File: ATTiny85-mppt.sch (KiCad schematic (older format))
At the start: 51 parts, among them J1 S+, J2 S-, J3 O+, J4 O-, Q1 BUK9511-55A127, Q2 BUK9511-55A127, Q3 2N2222A, Q4 2N2222A, Q5 2N2907A, Q6 2N2222A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

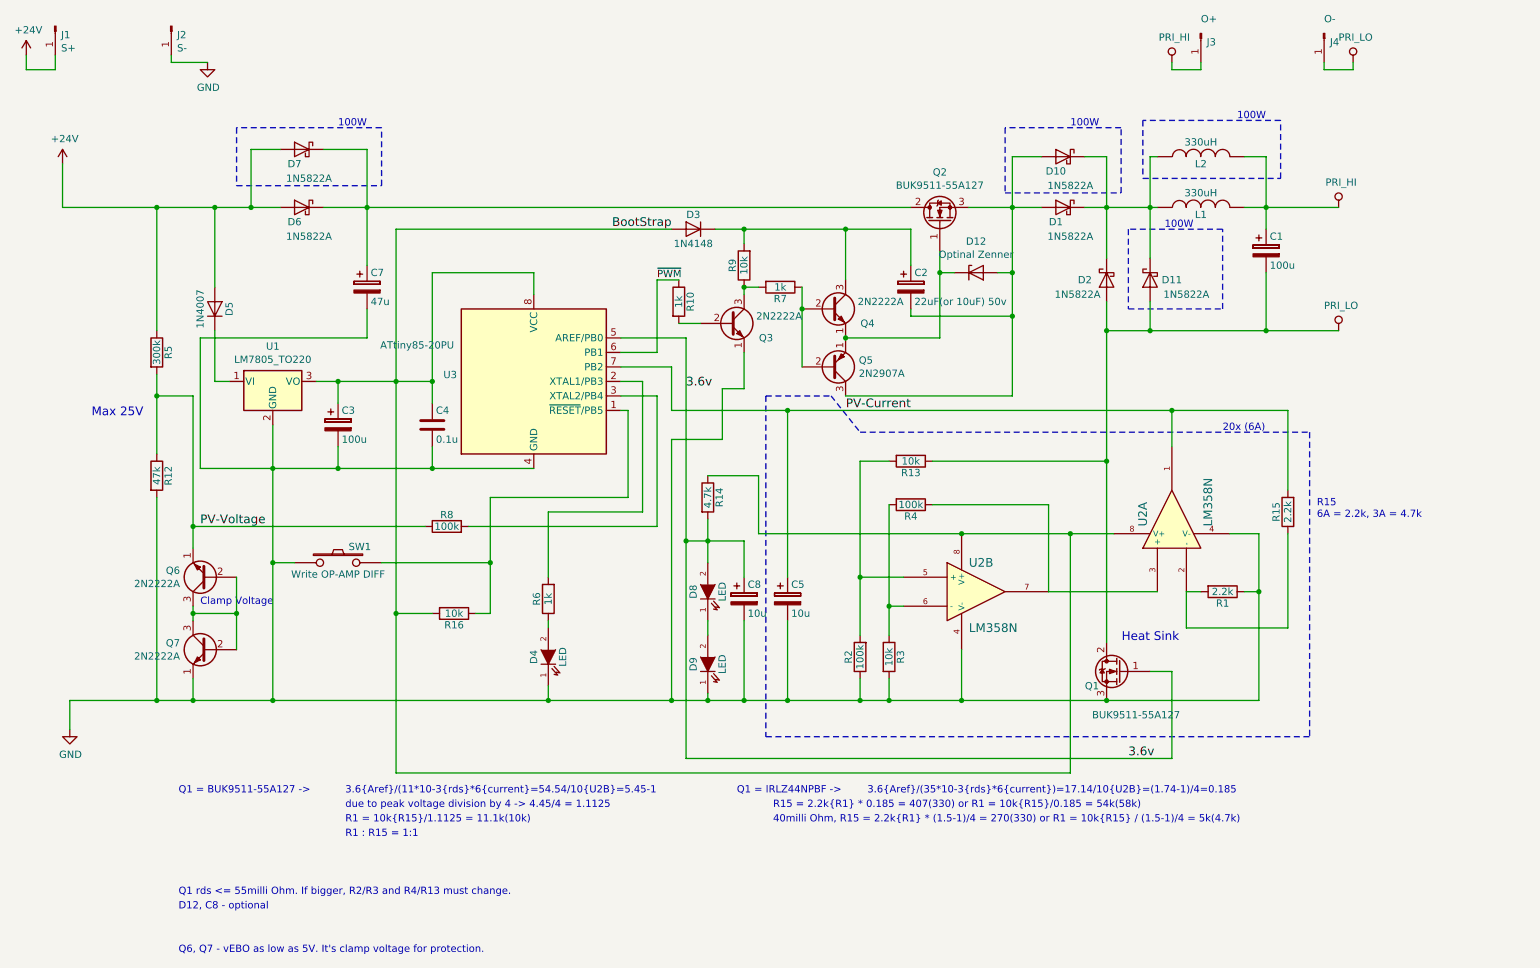
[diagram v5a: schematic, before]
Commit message: Update circuit. Limit load when control circuit voltage is low.
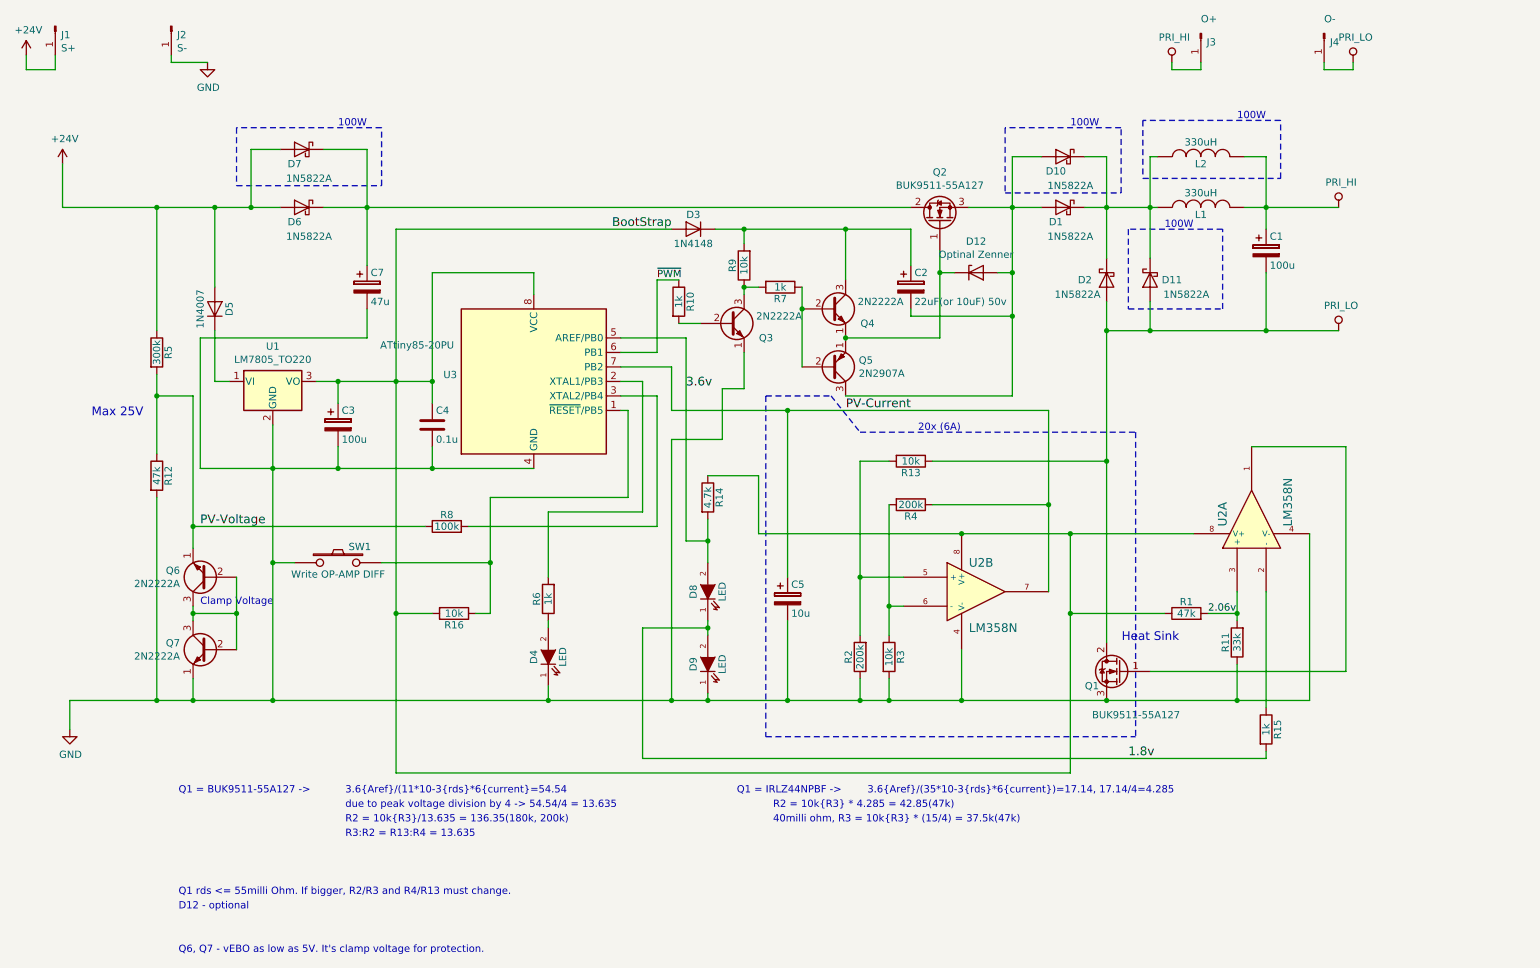
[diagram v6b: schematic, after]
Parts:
- removed C8: 10u, Capacitors_THT:CP_Radial_D12.5mm_P5.00mm, symbol Device:CP
- added R11: 33k, Resistors_THT:R_Axial_DIN0309_L9.0mm_D3.2mm_P12.70mm_Horizontal, symbol Device:R
- R1: value 2.2k -> 47k
- R15: value 2.2k -> 1k
- R2, R4: value 100k -> 200k
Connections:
- net 3.6v: no longer Q1.1 (G)
- net BootStrap: now also R1.1
- net GND: now also R11.1; no longer R1.1
- net PV-Current: now also R4.1, U2.7; no longer R15.2, U2.1
- net 1.8v: now reaches D8.1 (K), D9.2 (A)
- net 1.8v: now also R15.2
- net at R15.1, U2.2 (-): no longer R1.2
- new net: Q1.1 (G), U2.1
- new net 2.06v: R1.2, R11.2, U2.3 (+)
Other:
- note added: "3.6{Aref}/(11*10-3{rds}*6{current}=54.54"
- note added: "3.6{Aref}/(35*10-3{rds}*6{current})=17.14, 17.14/4=4.285"
- note added: "40milli ohm, R3 = 10k{R3} * (15/4) = 37.5k(47k)"
- note added: "D12 - optional"
- note added: "R2 = 10k{R3} * 4.285 = 42.85(47k)"
- note added: "R2 = 10k{R3}/13.635 = 136.35(180k, 200k)"
- note added: "R3:R2 = R13:R4 = 13.635"
- note added: "due to peak voltage division by 4 -> 54.54/4 = 13.635"
- note removed: "3.6{Aref}/(11*10-3{rds}*6{current}=54.54/10{U2B}=5.45-1"
- note removed: "3.6{Aref}/(35*10-3{rds}*6{current})=17.14/10{U2B}=(1.74-1)/4=0.185"
- note removed: "40milli Ohm, R15 = 2.2k{R1} * (1.5-1)/4 = 270(330) or R1 = 10k{R15} / (1.5-1)/4 = 5k(4.7k)"
- note removed: "D12, C8 - optional"
- note removed: "R1 : R15 = 1:1"
- note removed: "R1 = 10k{R15}/1.1125 = 11.1k(10k)"
- note removed: "R15 = 2.2k{R1} * 0.185 = 407(330) or R1 = 10k{R15}/0.185 = 54k(58k)"
- note removed: "R15\n6A = 2.2k, 3A = 4.7k"
- note removed: "due to peak voltage division by 4 -> 4.45/4 = 1.1125"
- moved on the sheet: R1, R15, U2A
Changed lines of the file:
@@
 Sheet 1 1
 Title "Simple MPPT with ATTiny85"
-Date "2018-12-26"
-Rev "1.9"
+Date "2019-02-06"
+Rev "2.0"
 Comp ""
 Comment1 ""
@@
 P 7050 4250
 F 0 "R4" V 7130 4250 50  0000 C CNN
-F 1 "100k" V 7050 4250 50  0000 C CNN
+F 1 "200k" V 7050 4250 50  0000 C CNN
 F 2 "Resistors_THT:R_Axial_DIN0309_L9.0mm_D3.2mm_P12.70mm_Horizontal" V 6980 4250 30  0001 C CNN
 F 3 "" H 7050 4250 30  0000 C CNN
@@
 P 6700 5300
 F 0 "R2" V 6780 5300 50  0000 C CNN
-F 1 "100k" V 6700 5300 50  0000 C CNN
+F 1 "200k" V 6700 5300 50  0000 C CNN
 F 2 "Resistors_THT:R_Axial_DIN0309_L9.0mm_D3.2mm_P12.70mm_Horizontal" V 6630 5300 30  0001 C CNN
 F 3 "" H 6700 5300 30  0000 C CNN
@@
 $EndComp
 Text Label 8550 6000 0    60   ~ 0
-3.6v
-$Comp
-L ATTiny85-mppt-rescue:LM358N-RESCUE-12f675-mppt-12f675-mppt-rescue U2
-U 1 1 56E669E2
-P 8850 4350
-F 0 "U2" H 8800 4550 60  0000 L CNN
-F 1 "LM358N" H 8800 4100 60  0000 L CNN
-F 2 "Housings_DIP:DIP-8_W7.62mm" H 8850 4350 60  0001 C CNN
-F 3 "" H 8850 4350 60  0000 C CNN
-	1    8850 4350
-	0    -1   -1   0
-$EndComp
+1.8v
 $Comp
 L Device:R R1
 U 1 1 56E67518
-P 9200 4850
-F 0 "R1" V 9280 4850 50  0000 C CNN
-F 1 "2.2k" V 9200 4850 50  0000 C CNN
-F 2 "Resistors_THT:R_Axial_DIN0309_L9.0mm_D3.2mm_P12.70mm_Horizontal" V 9130 4850 50  0001 C CNN
-F 3 "" H 9200 4850 50  0000 C CNN
-	1    9200 4850
-	0    1    1    0
+P 8950 5000
+F 0 "R1" V 9030 5000 50  0000 C CNN
+F 1 "47k" V 8950 5000 50  0000 C CNN
+F 2 "Resistors_THT:R_Axial_DIN0309_L9.0mm_D3.2mm_P12.70mm_Horizontal" V 8880 5000 50  0001 C CNN
+F 3 "" H 8950 5000 50  0000 C CNN
+	1    8950 5000
+	0    -1   -1   0
 $EndComp
 $Comp
 L Device:R R15
 U 1 1 56E68956
-P 9650 4300
-F 0 "R15" V 9730 4300 50  0000 C CNN
-F 1 "2.2k" V 9650 4300 50  0000 C CNN
-F 2 "Resistors_THT:R_Axial_DIN0309_L9.0mm_D3.2mm_P12.70mm_Horizontal" V 9580 4300 50  0001 C CNN
-F 3 "" H 9650 4300 50  0000 C CNN
-	1    9650 4300
-	-1   0    0    1
+P 9500 5800
+F 0 "R15" V 9580 5800 50  0000 C CNN
+F 1 "1k" V 9500 5800 50  0000 C CNN
+F 2 "Resistors_THT:R_Axial_DIN0309_L9.0mm_D3.2mm_P12.70mm_Horizontal" V 9430 5800 50  0001 C CNN
+F 3 "" H 9500 5800 50  0000 C CNN
+	1    9500 5800
+	1    0    0    -1
 $EndComp
 Wire Wire Line
@@
 Connection ~ 9500 2200
 Wire Notes Line
-	6050 5850 9800 5850
+	6050 5850 8600 5850
 Wire Wire Line
 	1850 4200 1850 5600
@@
 	5650 4350 5650 4500
 Wire Wire Line
-	5650 5050 5650 5150
+	5650 5050 5650 5100
 Wire Wire Line
 	5650 5550 5650 5600
@@
 Wire Wire Line
 	6200 4750 6200 3600
-Connection ~ 6200 3600
 Wire Notes Line
 	6050 3500 6050 5850
@@
 	6500 3500 6700 3750
 Wire Notes Line
-	6700 3750 9800 3750
+	6700 3750 8600 3750
 Wire Wire Line
 	3500 6100 8150 6100
-Wire Wire Line
-	8150 6100 8150 4450
 Wire Wire Line
 	4550 4300 4550 4750
@@
 	6000 4050 6000 4450
 Wire Wire Line
-	8850 5400 8700 5400
-Wire Wire Line
-	5500 6000 8850 6000
-Wire Wire Line
-	8850 6000 8850 5400
-Connection ~ 5500 4500
-Wire Wire Line
 	6000 4450 7400 4450
 Wire Wire Line
-	9450 5600 8400 5600
+	9800 5600 9300 5600
 Wire Wire Line
 	8000 4250 8000 4850
-Wire Wire Line
-	8000 4850 8750 4850
-Wire Wire Line
-	8850 3850 8850 3600
-Wire Wire Line
-	9450 4450 9450 4850
 Connection ~ 8400 5600
-Wire Wire Line
-	9050 4850 8950 4850
-Wire Wire Line
-	9450 4450 9250 4450
-Connection ~ 9450 4850
 Connection ~ 8150 4450
-Wire Wire Line
-	9650 5100 9650 4450
-Wire Wire Line
-	9650 3600 9650 4150
-Connection ~ 8850 3600
-Wire Notes Line
-	9800 3750 9800 5850
-Wire Wire Line
-	9350 4850 9450 4850
-Wire Wire Line
-	9650 5100 8950 5100
-Wire Wire Line
-	8950 5100 8950 4850
+Wire Notes Line
+	8600 3750 8600 5850
 $Comp
 L Device:CP C7
@@
 	5650 4500 5650 4650
 Wire Wire Line
-	5500 4500 5500 6000
-Wire Wire Line
 	8400 5600 7400 5600
 Wire Wire Line
-	9450 4850 9450 5600
-Wire Wire Line
-	8150 4450 8450 4450
-Wire Wire Line
-	8850 3600 9650 3600
+	8150 4450 9000 4450
 Wire Wire Line
 	3300 2200 3000 2200
@@
 Wire Wire Line
 	5200 3400 5050 3400
-Wire Wire Line
-	5650 5600 5900 5600
 Wire Wire Line
 	5500 3100 5500 4500
@@
 Wire Notes Line
 	9200 2350 8550 2350
-Text Notes 9200 3750 0    50   ~ 0
+Text Notes 7100 3750 0    50   ~ 0
 20x (6A)
 Text Notes 3100 1650 0    50   ~ 0
@@
 Q1 = IRLZ44NPBF ->
 Text Notes 6750 6250 0    50   ~ 0
-3.6{Aref}/(35*10-3{rds}*6{current})=17.14/10{U2B}=(1.74-1)/4=0.185
+3.6{Aref}/(35*10-3{rds}*6{current})=17.14, 17.14/4=4.285
 Text Notes 6100 6350 0    50   ~ 0
-R15 = 2.2k{R1} * 0.185 = 407(330) or R1 = 10k{R15}/0.185 = 54k(58k)
+R2 = 10k{R3} * 4.285 = 42.85(47k)
 Text Notes 2000 6250 0    50   ~ 0
 Q1 = BUK9511-55A127 ->
 Text Notes 3150 6250 0    50   ~ 0
-3.6{Aref}/(11*10-3{rds}*6{current}=54.54/10{U2B}=5.45-1
+3.6{Aref}/(11*10-3{rds}*6{current}=54.54
 Text Notes 3150 6450 0    50   ~ 0
-R1 = 10k{R15}/1.1125 = 11.1k(10k)
+R2 = 10k{R3}/13.635 = 136.35(180k, 200k)
 Text Notes 6100 6450 0    50   ~ 0
-40milli Ohm, R15 = 2.2k{R1} * (1.5-1)/4 = 270(330) or R1 = 10k{R15} / (1.5-1)/4 = 5k(4.7k)
+40milli ohm, R3 = 10k{R3} * (15/4) = 37.5k(47k)
 Text Notes 2000 6950 0    50   ~ 0
 Q1 rds <= 55milli Ohm. If bigger, R2/R3 and R4/R13 must change.
@@
 	5450 3000 5600 3000
 $Comp
-L Device:CP C8
-U 1 1 5BE62CB0
-P 5900 4900
-F 0 "C8" H 5925 5000 50  0000 L CNN
-F 1 "10u" H 5925 4800 50  0000 L CNN
-F 2 "Capacitors_THT:CP_Radial_D12.5mm_P5.00mm" H 5938 4750 30  0001 C CNN
-F 3 "" H 5900 4900 60  0000 C CNN
-	1    5900 4900
-	1    0    0    -1
-$EndComp
-Wire Wire Line
-	5900 4750 5900 4500
-Wire Wire Line
-	5900 4500 5650 4500
-Wire Wire Line
-	5900 5050 5900 5600
-Connection ~ 5900 5600
-Wire Wire Line
-	5900 5600 6200 5600
-$Comp
 L Device:D_Zener D12
 U 1 1 5BEB0C16
@@
 	5050 3100 5500 3100
 Wire Wire Line
-	6200 3600 8850 3600
-Wire Wire Line
 	6600 3100 7250 3100
 Text Notes 2000 7050 0    50   ~ 0
-D12, C8 - optional
+D12 - optional
 Wire Wire Line
 	2650 5600 4550 5600
@@
 	4000 4400 5300 4400
 Text Notes 3150 6350 0    50   ~ 0
-due to peak voltage division by 4 -> 4.45/4 = 1.1125
+due to peak voltage division by 4 -> 54.54/4 = 13.635
 Text Notes 3150 6550 0    50   ~ 0
-R1 : R15 = 1:1
-Text Notes 9850 4350 0    50   ~ 0
-R15\n6A = 2.2k, 3A = 4.7k
+R3:R2 = R13:R4 = 13.635
 $Comp
 L Device:Q_NPN_EBC Q6
@@
 Text Notes 2000 7350 0    50   ~ 0
 Q6, Q7 - vEBO as low as 5V. It's clamp voltage for protection.
+Wire Wire Line
+	8000 4250 8000 3600
+Wire Wire Line
+	8000 3600 6200 3600
+Connection ~ 8000 4250
+Connection ~ 6200 3600
+Wire Wire Line
+	9800 4450 9800 5600
+$Comp
+L ATTiny85-mppt-rescue:LM358N-RESCUE-12f675-mppt-12f675-mppt-rescue U2
+U 1 1 56E669E2
+P 9400 4350
+F 0 "U2" H 9350 4550 60  0000 L CNN
+F 1 "LM358N" H 9350 4100 60  0000 L CNN
+F 2 "Housings_DIP:DIP-8_W7.62mm" H 9400 4350 60  0001 C CNN
+F 3 "" H 9400 4350 60  0000 C CNN
+	1    9400 4350
+	0    -1   -1   0
+$EndComp
+Wire Wire Line
+	9400 3850 10050 3850
+Wire Wire Line
+	10050 3850 10050 5400
+Wire Wire Line
+	10050 5400 8700 5400
+Wire Wire Line
+	8150 4450 8150 5000
+Wire Wire Line
+	8800 5000 8150 5000
+Connection ~ 8150 5000
+Wire Wire Line
+	8150 5000 8150 6100
+Wire Wire Line
+	9300 4850 9300 5000
+Wire Wire Line
+	9100 5000 9300 5000
+Wire Wire Line
+	5650 5100 5200 5100
+Wire Wire Line
+	5200 5100 5200 6000
+Wire Wire Line
+	5200 6000 9500 6000
+Wire Wire Line
+	9500 6000 9500 5950
+Connection ~ 5650 5100
+Wire Wire Line
+	5650 5100 5650 5150
+Wire Wire Line
+	9500 4850 9500 5650
+$Comp
+L Device:R R11
+U 1 1 5C6A7369
+P 9300 5200
+F 0 "R11" V 9380 5200 50  0000 C CNN
+F 1 "33k" V 9300 5200 50  0000 C CNN
+F 2 "Resistors_THT:R_Axial_DIN0309_L9.0mm_D3.2mm_P12.70mm_Horizontal" V 9230 5200 50  0001 C CNN
+F 3 "" H 9300 5200 50  0000 C CNN
+	1    9300 5200
+	-1   0    0    1
+$EndComp
+Wire Wire Line
+	9300 5000 9300 5050
+Connection ~ 9300 5000
+Wire Wire Line
+	9300 5350 9300 5600
+Connection ~ 9300 5600
+Wire Wire Line
+	9300 5600 8400 5600
+Text Label 9100 5000 0    50   ~ 0
+2.06v
+Wire Wire Line
+	5650 5600 6200 5600
 $EndSCHEMATC

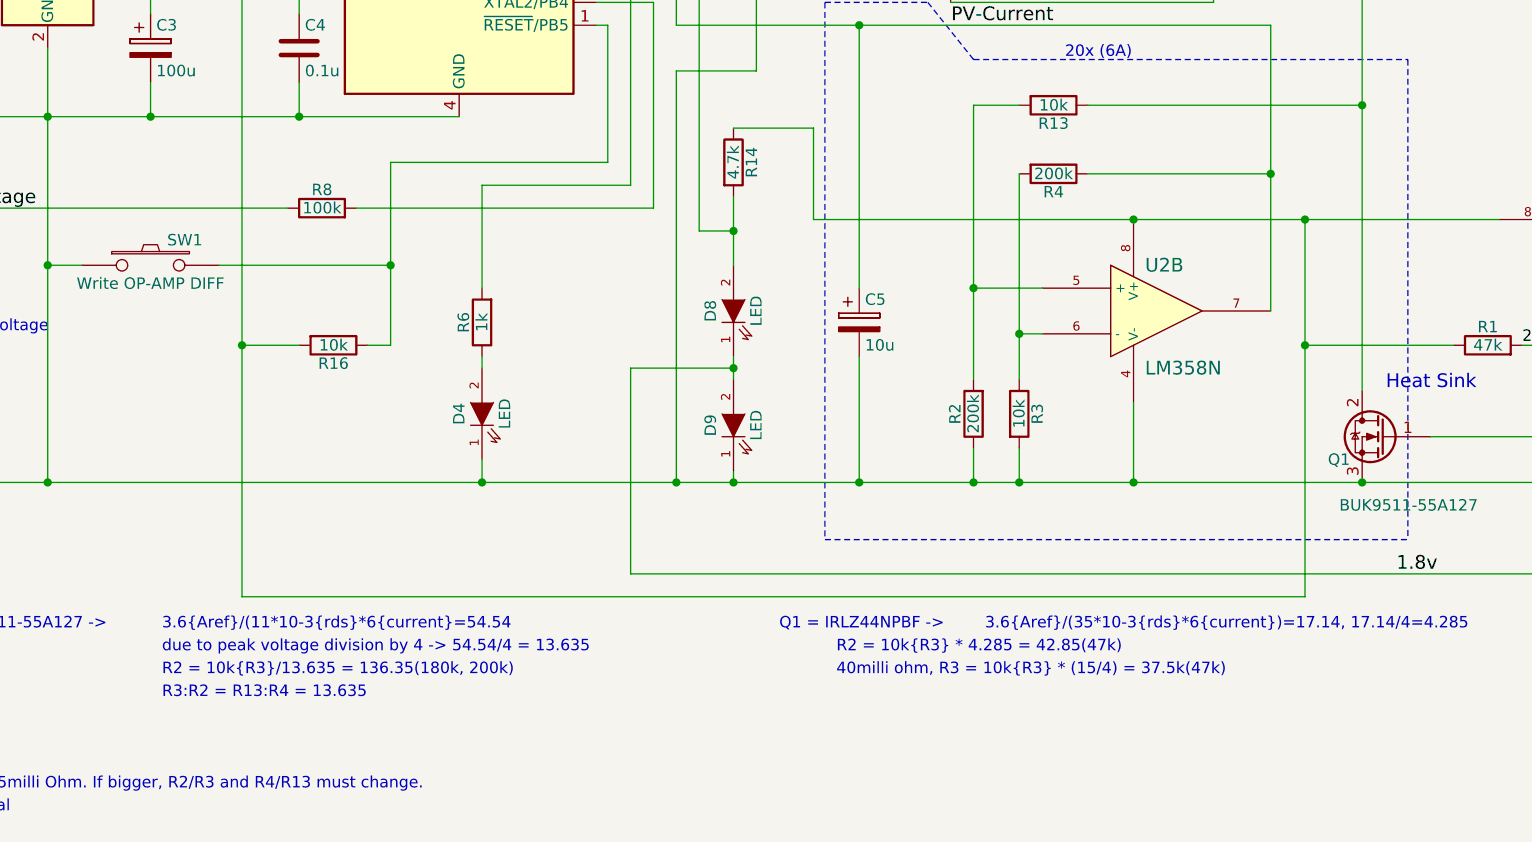
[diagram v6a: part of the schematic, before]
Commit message: Fix resistor values.
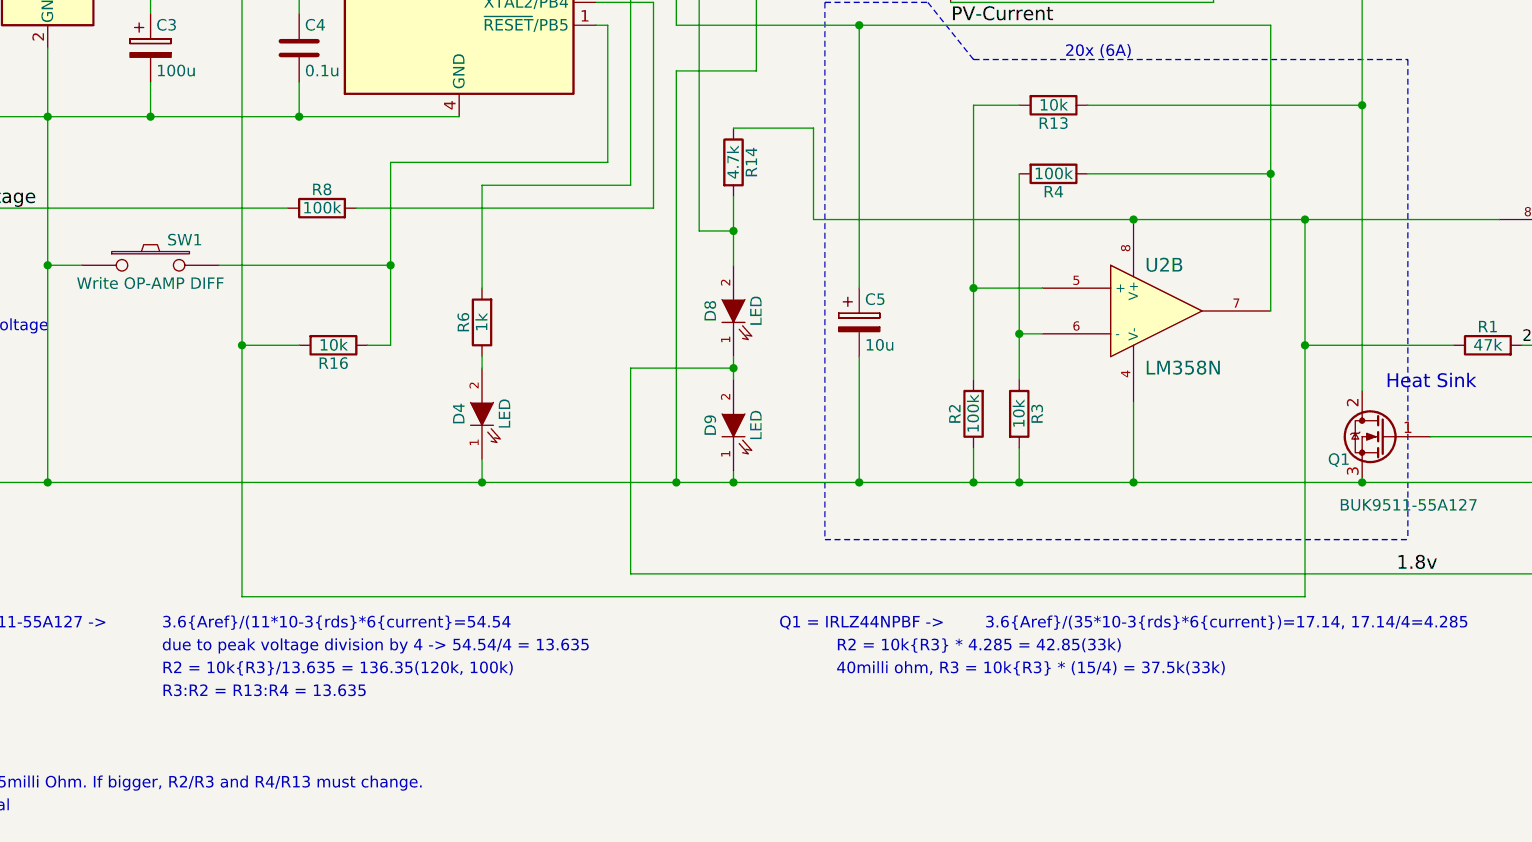
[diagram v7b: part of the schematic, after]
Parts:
- R2, R4: value 200k -> 100k
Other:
- note added: "40milli ohm, R3 = 10k{R3} * (15/4) = 37.5k(33k)"
- note added: "R2 = 10k{R3} * 4.285 = 42.85(33k)"
- note added: "R2 = 10k{R3}/13.635 = 136.35(120k, 100k)"
- note removed: "40milli ohm, R3 = 10k{R3} * (15/4) = 37.5k(47k)"
- note removed: "R2 = 10k{R3} * 4.285 = 42.85(47k)"
- note removed: "R2 = 10k{R3}/13.635 = 136.35(180k, 200k)"
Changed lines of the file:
@@
 Sheet 1 1
 Title "Simple MPPT with ATTiny85"
-Date "2019-02-06"
-Rev "2.0"
+Date "2019-02-09"
+Rev "2.1"
 Comp ""
 Comment1 ""
@@
 P 7050 4250
 F 0 "R4" V 7130 4250 50  0000 C CNN
-F 1 "200k" V 7050 4250 50  0000 C CNN
+F 1 "100k" V 7050 4250 50  0000 C CNN
 F 2 "Resistors_THT:R_Axial_DIN0309_L9.0mm_D3.2mm_P12.70mm_Horizontal" V 6980 4250 30  0001 C CNN
 F 3 "" H 7050 4250 30  0000 C CNN
@@
 P 6700 5300
 F 0 "R2" V 6780 5300 50  0000 C CNN
-F 1 "200k" V 6700 5300 50  0000 C CNN
+F 1 "100k" V 6700 5300 50  0000 C CNN
 F 2 "Resistors_THT:R_Axial_DIN0309_L9.0mm_D3.2mm_P12.70mm_Horizontal" V 6630 5300 30  0001 C CNN
 F 3 "" H 6700 5300 30  0000 C CNN
@@
 3.6{Aref}/(35*10-3{rds}*6{current})=17.14, 17.14/4=4.285
 Text Notes 6100 6350 0    50   ~ 0
-R2 = 10k{R3} * 4.285 = 42.85(47k)
+R2 = 10k{R3} * 4.285 = 42.85(33k)
 Text Notes 2000 6250 0    50   ~ 0
 Q1 = BUK9511-55A127 ->
@@
 3.6{Aref}/(11*10-3{rds}*6{current}=54.54
 Text Notes 3150 6450 0    50   ~ 0
-R2 = 10k{R3}/13.635 = 136.35(180k, 200k)
+R2 = 10k{R3}/13.635 = 136.35(120k, 100k)
 Text Notes 6100 6450 0    50   ~ 0
-40milli ohm, R3 = 10k{R3} * (15/4) = 37.5k(47k)
+40milli ohm, R3 = 10k{R3} * (15/4) = 37.5k(33k)
 Text Notes 2000 6950 0    50   ~ 0
 Q1 rds <= 55milli Ohm. If bigger, R2/R3 and R4/R13 must change.
